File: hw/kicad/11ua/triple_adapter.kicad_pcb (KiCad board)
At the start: 2 copper layers, 57 x 75 mm, 78 parts, among them J1 RJ45, J2 RJ45, J3 CONN_01X04, J4 CONN_01X04, U1 LM339

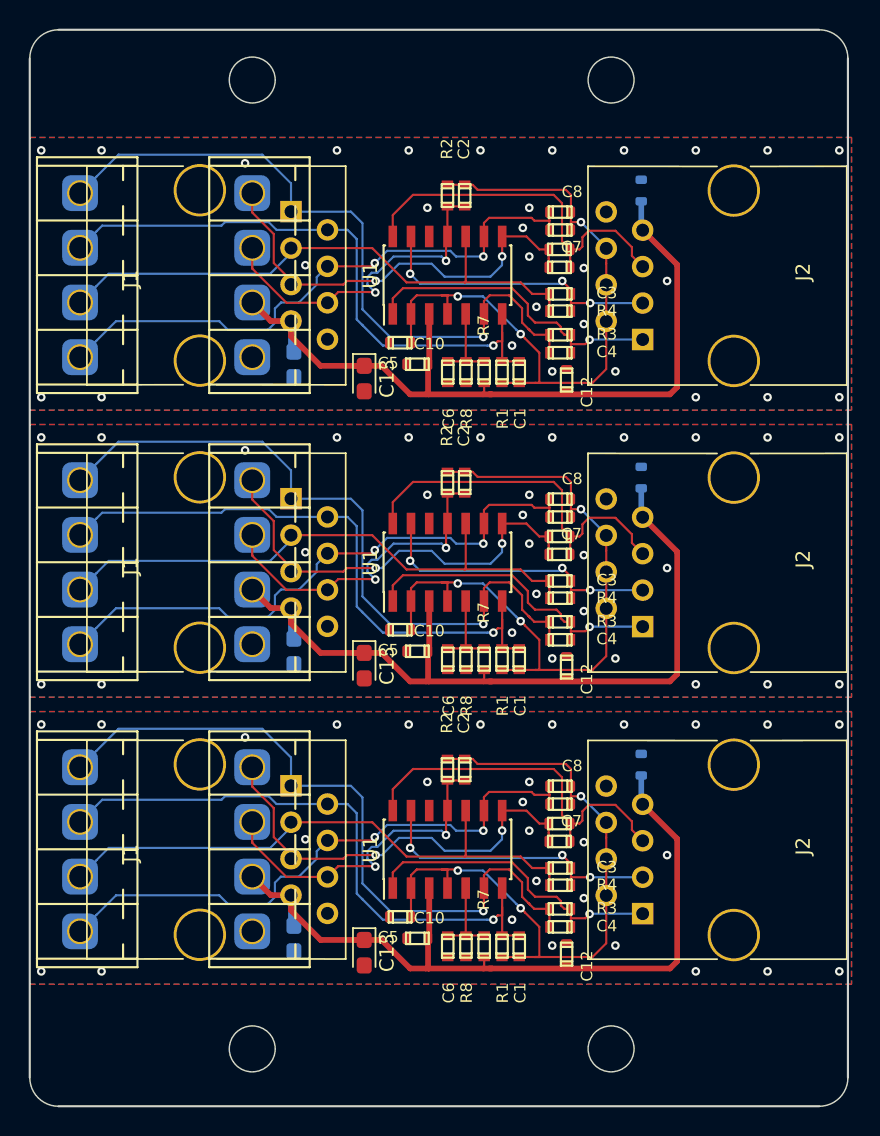
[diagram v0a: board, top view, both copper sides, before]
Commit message: change rj45
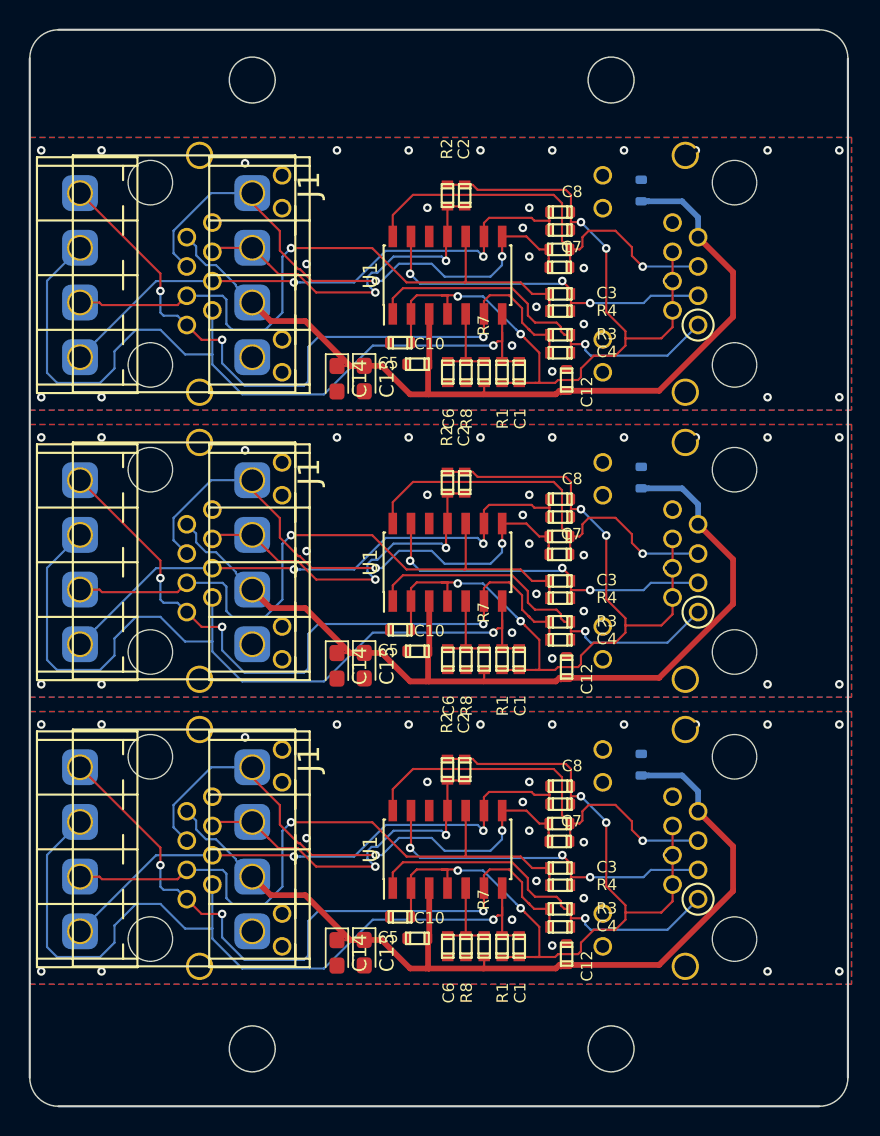
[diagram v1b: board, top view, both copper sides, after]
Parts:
- removed the C14 at (145.8, 82.7)
- removed the C14 at (145.8, 122.7)
- removed the J1 at (145.6, 72.1)
- removed the J1 at (145.6, 112.1)
- removed the J1 at (145.6, 92.1)
- removed the J2 at (170.1, 81.0)
- removed the J2 at (170.1, 121.0)
- removed the J2 at (170.1, 101.0)
- added C14: CP, Capacitor_Tantalum_SMD:CP_EIA-2012-15_AVX-P, F.Cu at (148.8, 83.7)
- added C14: CP, Capacitor_Tantalum_SMD:CP_EIA-2012-15_AVX-P, F.Cu at (148.8, 103.7)
- added J1: RJ45_LED, stmbl:RJ45_LED, F.Cu at (130.4, 76.4)
- added J1: RJ45_LED, stmbl:RJ45_LED, F.Cu at (130.4, 96.4)
- added J1: RJ45_LED, stmbl:RJ45_LED, F.Cu at (130.4, 116.4)
- added J2: RJ45_LED, stmbl:RJ45_LED, B.Cu at (181.9, 76.4)
- added J2: RJ45_LED, stmbl:RJ45_LED, B.Cu at (181.9, 96.4)
- added J2: RJ45_LED, stmbl:RJ45_LED, B.Cu at (181.9, 116.4)
- C14: moved to F.Cu
- moved C14 21.2 mm to (148.8, 123.7)
- moved C1 20.0 mm to (161.5, 103.2)
- moved C1 20.0 mm to (161.5, 123.2)
- moved C10 20.0 mm to (154.4, 102.7)
- moved C10 20.0 mm to (154.4, 122.7)
- moved C11 20.0 mm to (170.0, 90.6)
- moved C11 20.0 mm to (170.0, 110.6)
- moved C12 20.0 mm to (164.8, 103.8)
- moved C12 20.0 mm to (164.8, 123.8)
- moved C13 20.0 mm to (150.7, 103.7)
- moved C13 20.0 mm to (150.7, 123.7)
- moved C2 20.0 mm to (157.7, 91.0)
- moved C2 20.0 mm to (157.7, 111.0)
- moved C3 20.0 mm to (164.3, 97.8)
- moved C3 20.0 mm to (164.3, 117.8)
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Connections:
- J4 pad 1: Net-(C7-Pad2) -> (no net)
- J4 pad 2: Net-(C2-Pad2) -> (no net)
- J4 pad 3: +5V -> (no net)
- J4 pad 4: GND -> (no net)
- J4 pad 1: (no net) -> Net-(C7-Pad2)
- J4 pad 2: (no net) -> Net-(C2-Pad2)
- J4 pad 3: (no net) -> +5V
- J4 pad 4: (no net) -> GND
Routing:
- net (no net): track 814.8 -> 933.7 mm, vias 86 -> 92
- net Net-(C1-Pad2): track 42.3 -> 55.9 mm
- net 2.5V: track 48.4 -> 58.6 mm, vias 3 -> 5
- net +5V: track 56.5 -> 65.5 mm
- net Net-(C7-Pad2): track 30.4 -> 38.7 mm
- net Net-(C4-Pad1): track 22.1 -> 27.4 mm
- net Net-(C3-Pad2): track 40.2 -> 45.4 mm, vias 0 -> 1
- net Net-(C3-Pad1): track 21.0 -> 25.0 mm
- net Net-(C7-Pad1): track 26.2 -> 30.0 mm, vias 0 -> 1
- net Net-(C2-Pad2): track 23.9 -> 25.3 mm
- net Net-(C8-Pad2): track 41.1 -> 39.8 mm
- net Net-(C4-Pad2): vias 1 -> 3
- net GND: vias 28 -> 25
